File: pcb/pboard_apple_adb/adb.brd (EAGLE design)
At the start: 56 x 65 mm, 24 parts, among them IC3 STM32F042F4, SW1 324_SW, SW2 324_SW, SW4 324_SW

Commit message: finishing touches for new boards
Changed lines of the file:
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@@
 <wire x1="16.51" y1="49.022" x2="16.51" y2="50.419" width="0.2032" layer="16"/>
 <wire x1="19.177" y1="46.355" x2="16.51" y2="49.022" width="0.2032" layer="16"/>
-<wire x1="34.7" y1="57.2" x2="36.047" y2="58.547" width="0.2032" layer="16"/>
-<wire x1="42.799" y1="58.547" x2="44.323" y2="57.023" width="0.2032" layer="16"/>
-<wire x1="44.323" y1="57.023" x2="44.323" y2="19.177" width="0.2032" layer="16"/>
+<wire x1="34.7" y1="57.2" x2="36.047" y2="58.547" width="0.254" layer="16"/>
+<wire x1="42.799" y1="58.547" x2="44.323" y2="57.023" width="0.254" layer="16"/>
+<wire x1="44.323" y1="57.023" x2="44.323" y2="19.177" width="0.254" layer="16"/>
 <via x="44.323" y="19.177" extent="1-16" drill="0.5"/>
-<wire x1="36.047" y1="58.547" x2="42.799" y2="58.547" width="0.2032" layer="16"/>
+<wire x1="36.047" y1="58.547" x2="42.799" y2="58.547" width="0.254" layer="16"/>
 <wire x1="49.04" y1="19.091" x2="49.04" y2="14.691" width="1.016" layer="1"/>
 <wire x1="49.04" y1="19.091" x2="48.954" y2="19.177" width="0.3048" layer="1"/>

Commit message: updated ADB board
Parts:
- removed JP2: (no value), pinhead:1X06
- added JP5: (no value), pinhead:1X05
- moved R2 16.5 mm to (19.9, 46.1), turned to 0 degrees
- moved R5 9.86 mm to (7.75, 43.9), turned to 90 degrees
- moved LED1 8.51 mm to (24.0, 46.1), turned to 90 degrees
- moved R1 0.25 mm to (12.8, 40.0)
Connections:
- removed net N$9: IC3.9, JP2.1, LED1.A
- net +3V3: now also JP5.4; no longer JP2.5
- net GND: now also JP5.5; no longer JP2.6
- net N$14: now also IC3.9
- net N$2: now also LED1.A
- net N$5: now also JP5.3; no longer JP2.4
- net N$6: now also JP5.2; no longer JP2.3
- net N$8: now also JP5.1; no longer JP2.2
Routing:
- net N$9: track 38.3 -> 0.00 mm
- net N$14: track 25.9 -> 47.5 mm, vias 0 -> 1
- net N$2: track 23.6 -> 26.6 mm
- net N$5: track 51.1 -> 49.2 mm
- net N$8: track 25.3 -> 24.8 mm
- net N$6: track 24.6 -> 24.0 mm
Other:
- board text added: "git.io/usb4vc dekuNukem JAN 2022 PT2"
- board text removed: "RX"
- board text removed: "git.io/usb4vc dekuNukem Dec 2021 PT1"

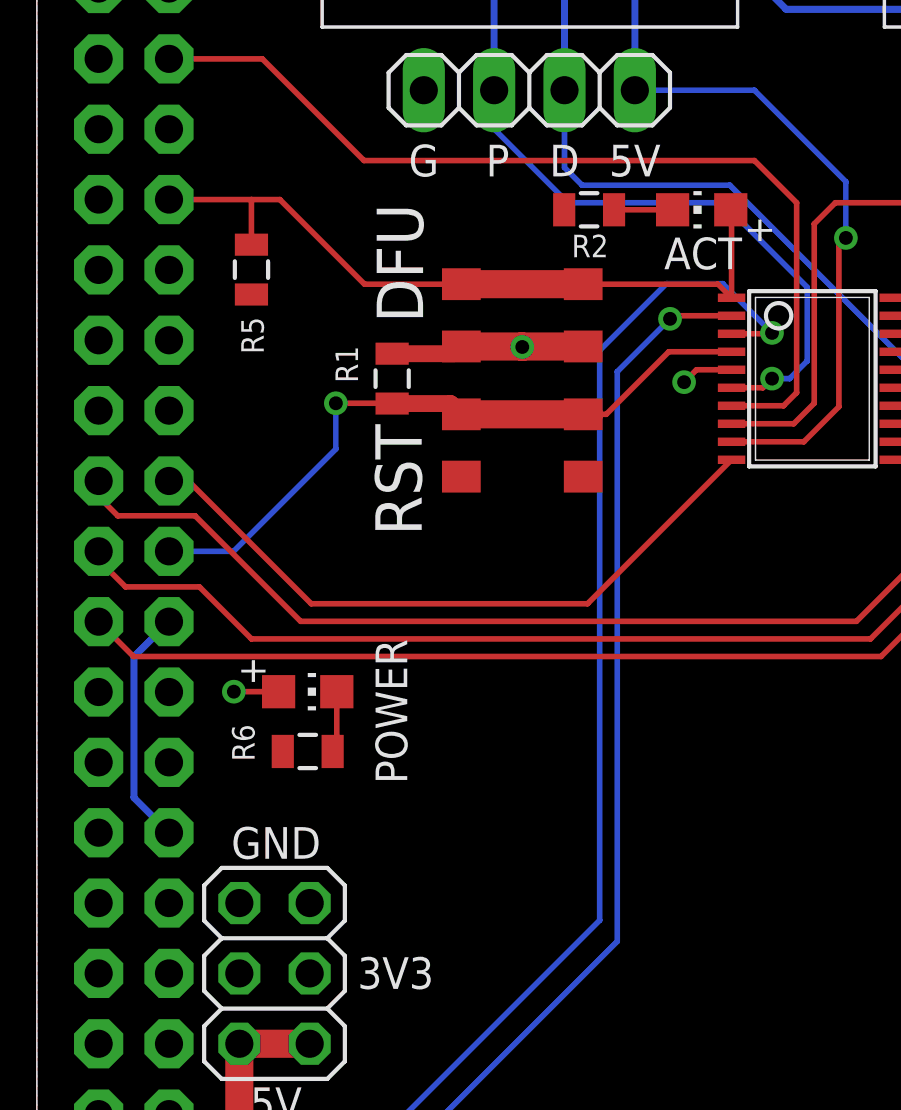
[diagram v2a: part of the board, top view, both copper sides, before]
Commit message: porting ADB code to new board
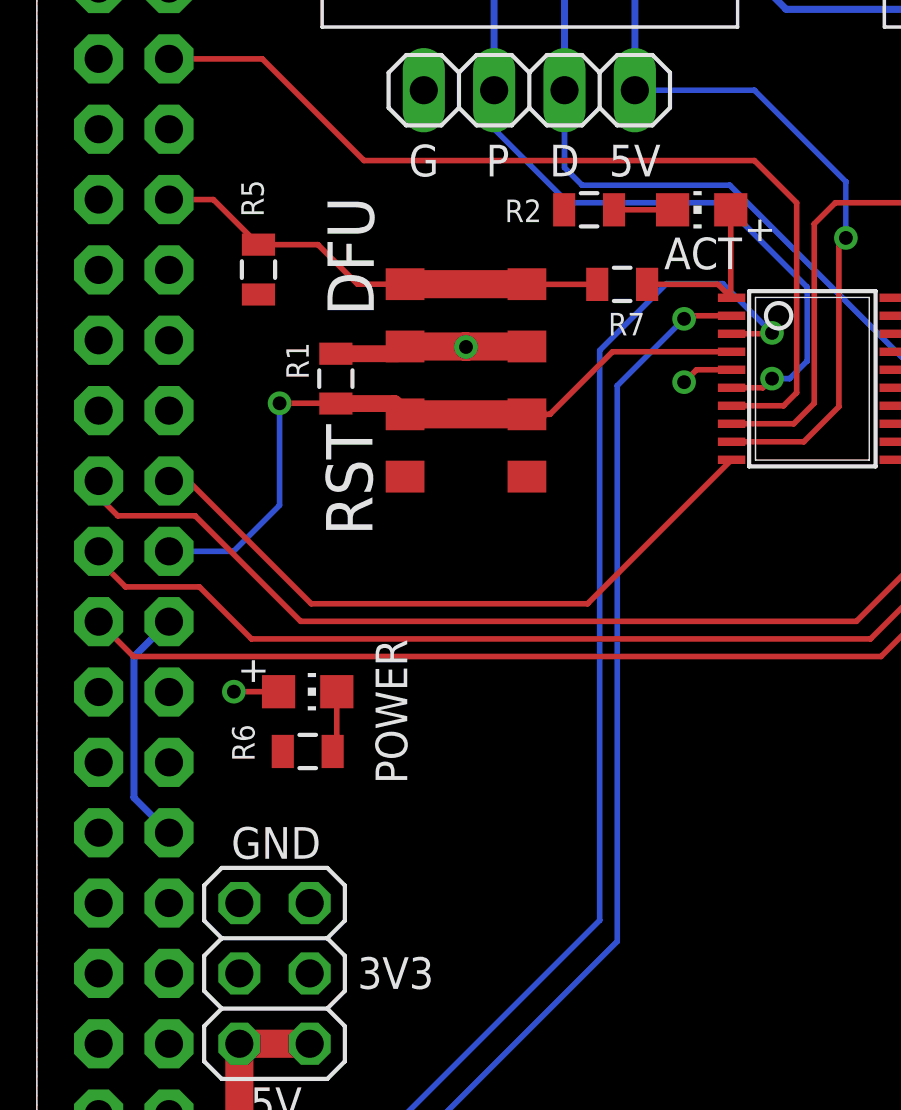
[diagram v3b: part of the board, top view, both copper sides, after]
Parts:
- added R7: 12K, SparkFun-Passives:0805
- moved R1 2.03 mm to (10.8, 40.0)
- moved SW1 2.03 mm to (15.5, 42.3)
- moved SW4 2.03 mm to (15.5, 37.6)
- moved R5 0.25 mm to (8.00, 43.9)
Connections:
- new net N$9: IC3.1, LED1.A, R7.2
- net N$2: now also R7.1; no longer IC3.1, LED1.A
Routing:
- net N$2: track 26.6 -> 16.7 mm
- net N$9: track 0.00 -> 6.44 mm
- net N$13: track 24.8 -> 26.0 mm

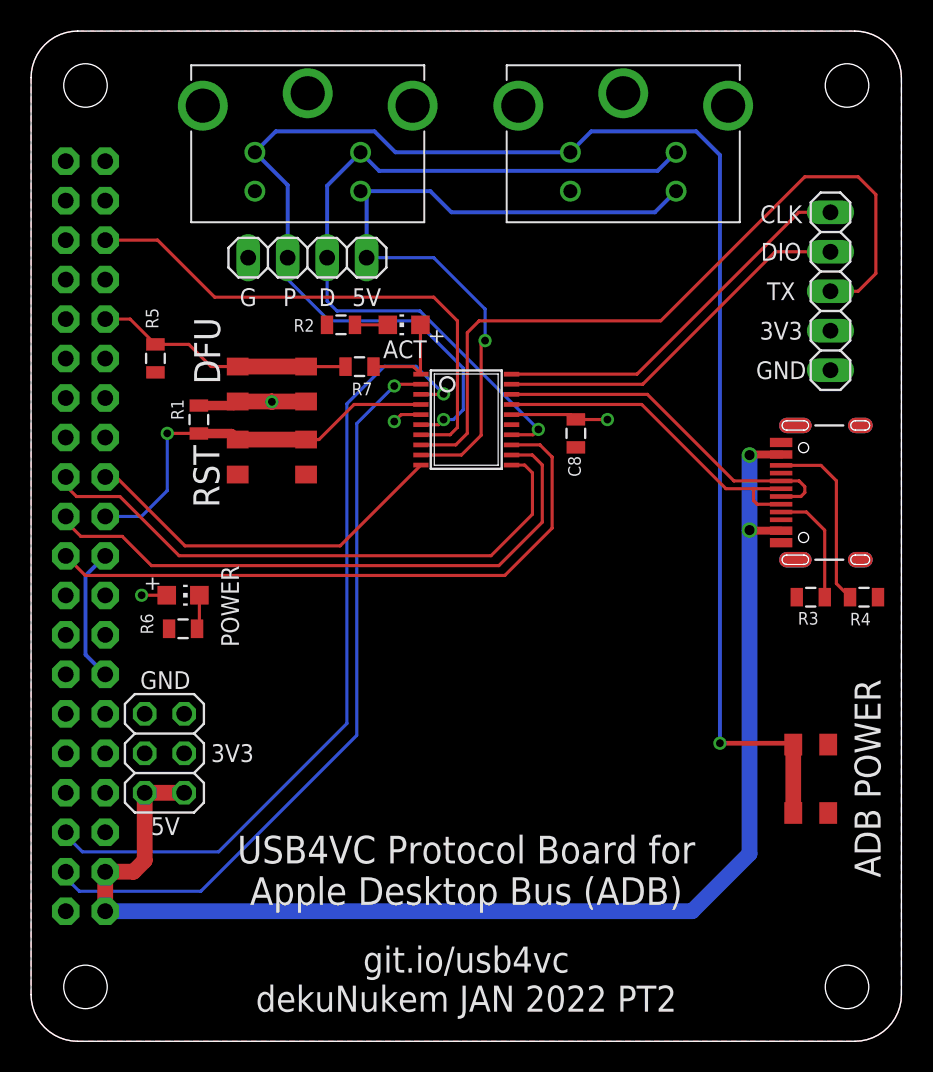
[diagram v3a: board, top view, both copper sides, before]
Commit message: fixed flipped ADB connector footprint
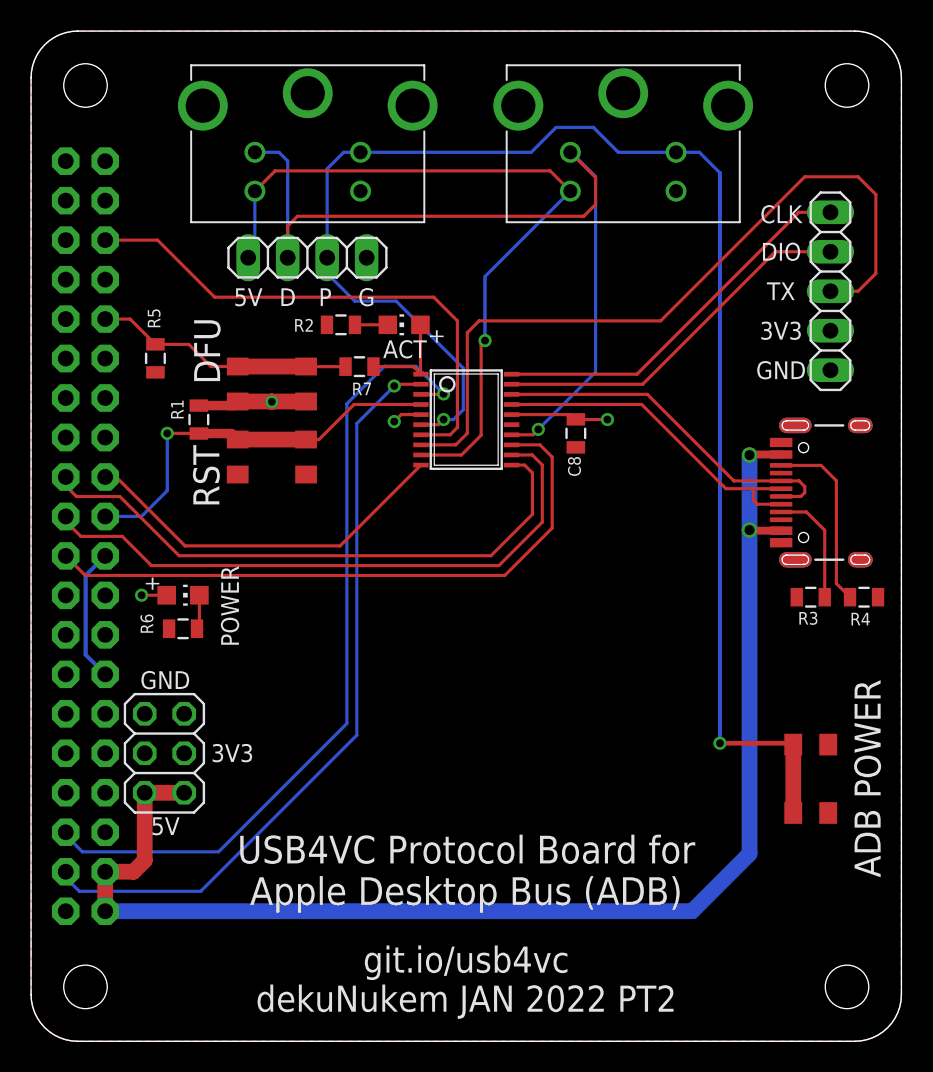
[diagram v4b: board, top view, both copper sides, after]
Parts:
- turned JP3 to 0 degrees
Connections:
- net GND: now also U$1.GND, U$6.GND; no longer U$1.4_GND, U$6.4_GND
- net N$14: now also U$1.5V, U$6.5V; no longer U$1.3_5V, U$6.3_5V
- net N$15: now also U$1.ADB, U$6.ADB; no longer U$1.1_ADB, U$6.1_ADB
- net N$18: now also U$1.PSW, U$6.PSW; no longer U$1.2_PSW, U$6.2_PSW
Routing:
- net N$18: track 107.7 -> 97.3 mm
- net N$15: track 50.6 -> 56.9 mm
- net N$14: track 47.5 -> 48.3 mm

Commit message: updated PCB for second prototype run
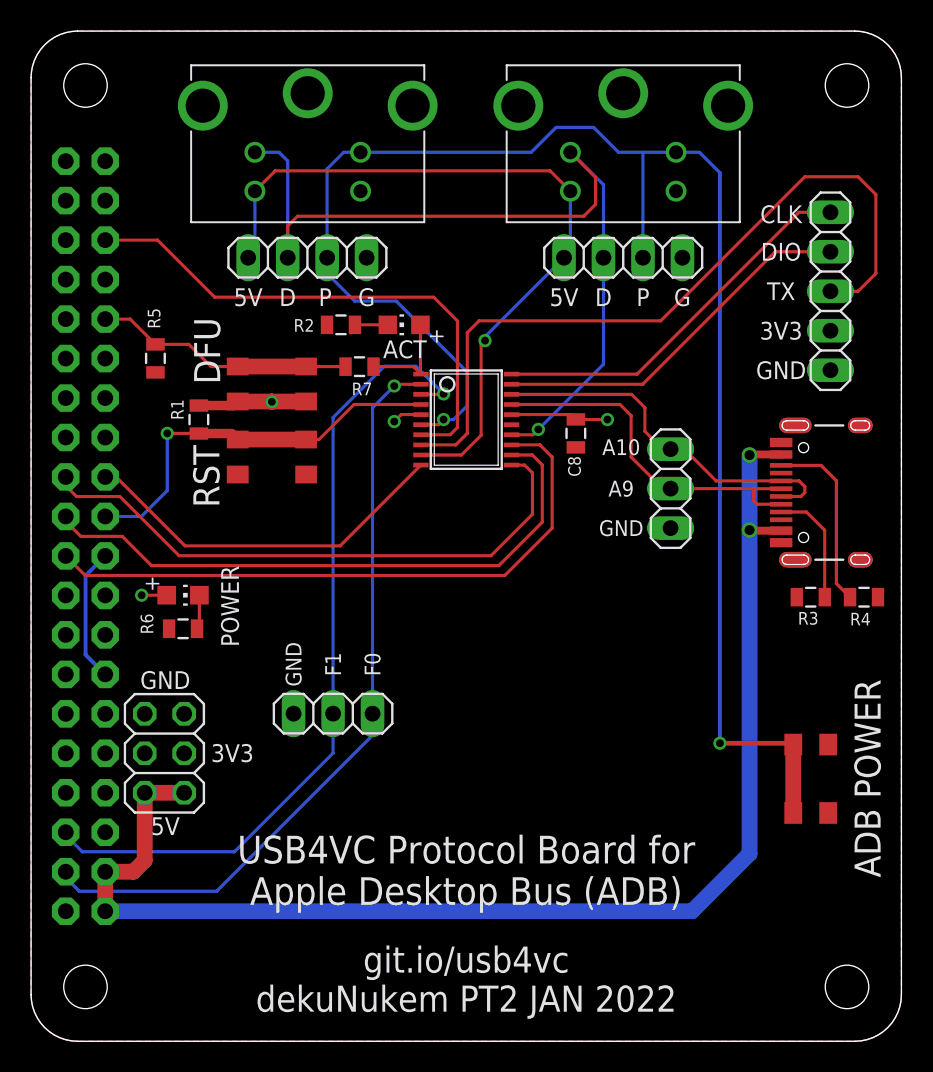
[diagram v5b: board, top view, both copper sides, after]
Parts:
- added JP2, JP6: (no value), pinhead:1X03
- added JP7: (no value), pinhead:1X04
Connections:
- net GND: now also JP2.1, JP7.4
- net N$10: now also JP6.1
- net N$11: now also JP6.2
- net N$14: now also JP7.1
- net N$15: now also JP7.2
- net N$18: now also JP7.3
- net N$3: now also JP2.3
- net N$4: now also JP2.2
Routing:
- net N$18: track 97.3 -> 104.3 mm
- net N$4: track 22.2 -> 23.8 mm
- net N$3: track 23.3 -> 24.2 mm
- net N$11: track 52.1 -> 52.7 mm
- net N$10: track 48.9 -> 49.5 mm
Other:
- board text added: "A10"
- board text added: "A9"
- board text added: "F0"
- board text added: "F1"
- board text added: "git.io/usb4vc dekuNukem PT2 JAN 2022"
- board text removed: "git.io/usb4vc dekuNukem JAN 2022 PT2"

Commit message: updated component values
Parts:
- R1, R5: value 12K -> 5.1K
- R3: value 5.1k -> 5.1K
- R4: value 5.1k -> 5.1kK
- R7: value 12K -> 2K
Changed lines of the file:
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@@
 <attribute name="NAME" x="7.8613" y="26.1874" size="0.8128" layer="25" rot="R90"/>
 </element>
-<element name="R1" library="SparkFun-Passives" package="0805" value="12K" x="10.795" y="40.005" smashed="yes" rot="R90">
+<element name="R1" library="SparkFun-Passives" package="0805" value="5.1K" x="10.795" y="40.005" smashed="yes" rot="R90">
 <attribute name="NAME" x="9.8171" y="39.9796" size="0.8128" layer="25" rot="R90"/>
 </element>
@@
 <attribute name="VALUE" x="52.07" y="35.306" size="0.762" layer="27" rot="R90" align="center"/>
 </element>
-<element name="R3" library="SparkFun-Passives" package="0805" value="5.1k" x="50.165" y="28.575" smashed="yes" rot="R180">
+<element name="R3" library="SparkFun-Passives" package="0805" value="5.1K" x="50.165" y="28.575" smashed="yes" rot="R180">
 <attribute name="NAME" x="50.673" y="27.6225" size="0.8128" layer="25" rot="R180"/>
 </element>
-<element name="R4" library="SparkFun-Passives" package="0805" value="5.1k" x="53.594" y="28.575" smashed="yes">
+<element name="R4" library="SparkFun-Passives" package="0805" value="5.1kK" x="53.594" y="28.575" smashed="yes">
 <attribute name="NAME" x="54.0258" y="27.5717" size="0.8128" layer="25" rot="R180"/>
 </element>
 <element name="SW1" library="3pos_slide_switch_centered" package="342_SWICH_FOOT" value="324_SW" x="15.494" y="42.291" smashed="yes" rot="R180"/>
-<element name="R5" library="SparkFun-Passives" package="0805" value="12K" x="8.001" y="43.942" smashed="yes" rot="R90">
+<element name="R5" library="SparkFun-Passives" package="0805" value="5.1K" x="8.001" y="43.942" smashed="yes" rot="R90">
 <attribute name="NAME" x="8.3185" y="45.847" size="0.8128" layer="25" rot="R90"/>
 </element>
@@
 <attribute name="VALUE" x="48.26" y="54.61" size="1.27" layer="27" rot="R270"/>
 </element>
-<element name="R7" library="SparkFun-Passives" package="0805" value="12K" x="21.1328" y="43.4086" smashed="yes">
+<element name="R7" library="SparkFun-Passives" package="0805" value="2K" x="21.1328" y="43.4086" smashed="yes">
 <attribute name="NAME" x="20.6248" y="41.5671" size="0.8128" layer="25"/>
 </element>
